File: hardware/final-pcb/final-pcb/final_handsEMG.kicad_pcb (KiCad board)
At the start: 2 copper layers, 109 parts, among them J1 Conn_02x13_Odd_Even, U1 ADS1299CPAG, U2 STM32L496ZGT6, U3 FT231XQ-R, U6 TPS60403DBVT, U8 TPS72325DBVT, U9 TPS73225DBVT

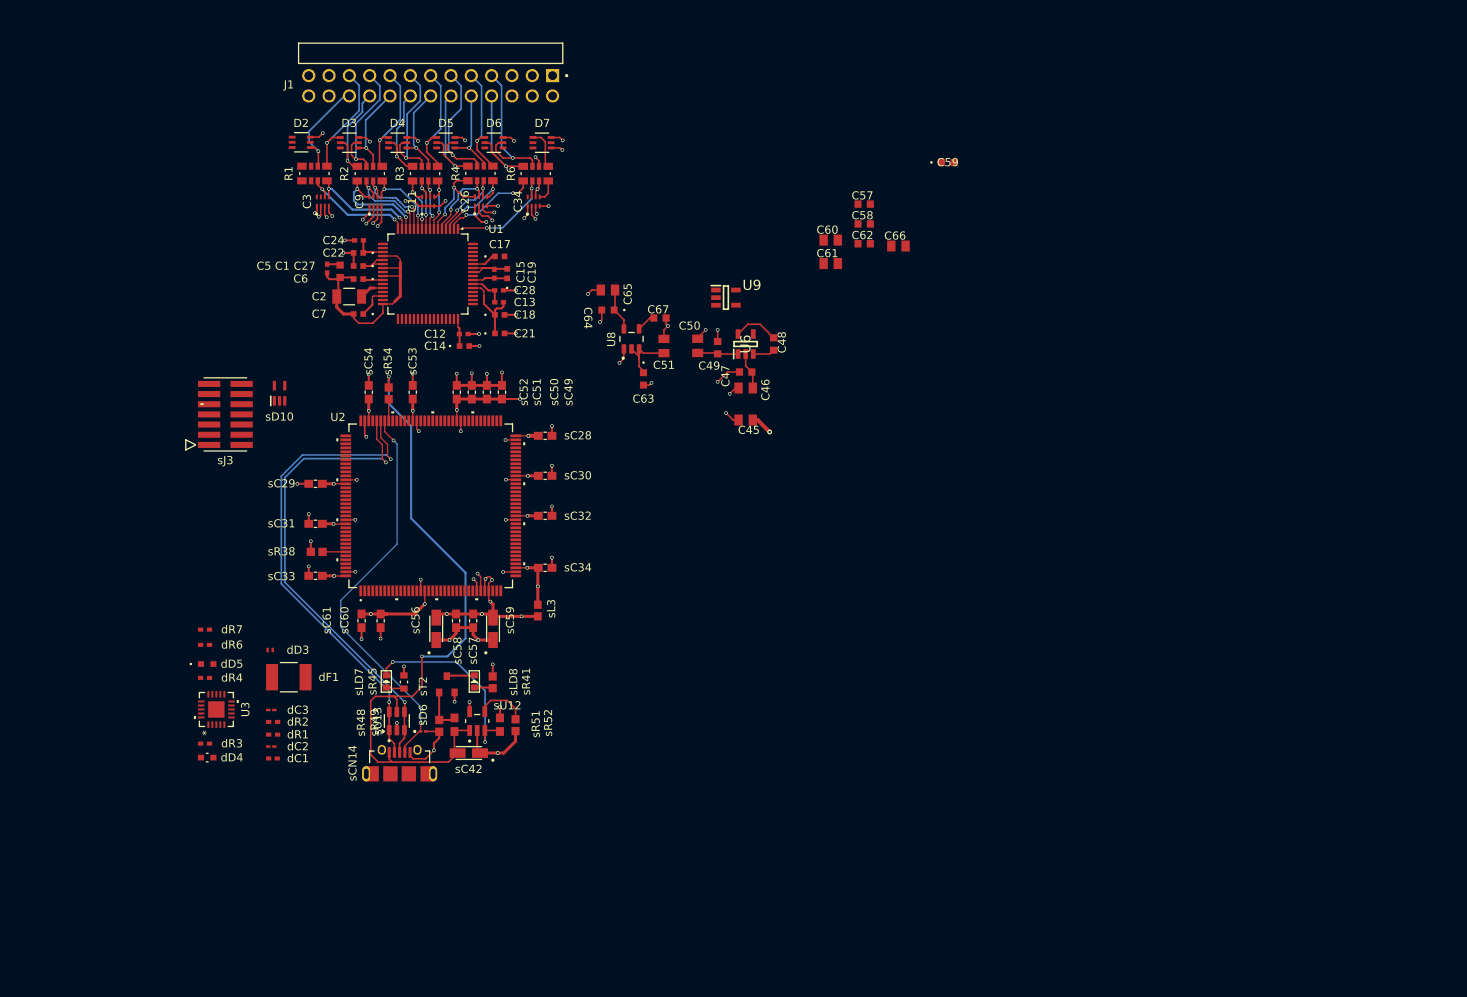
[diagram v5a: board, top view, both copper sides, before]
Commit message: 90% of components are placed (4.5.25)
NEED TESTPOINTS and configure the jumper parts for the PMIC without using jumpers
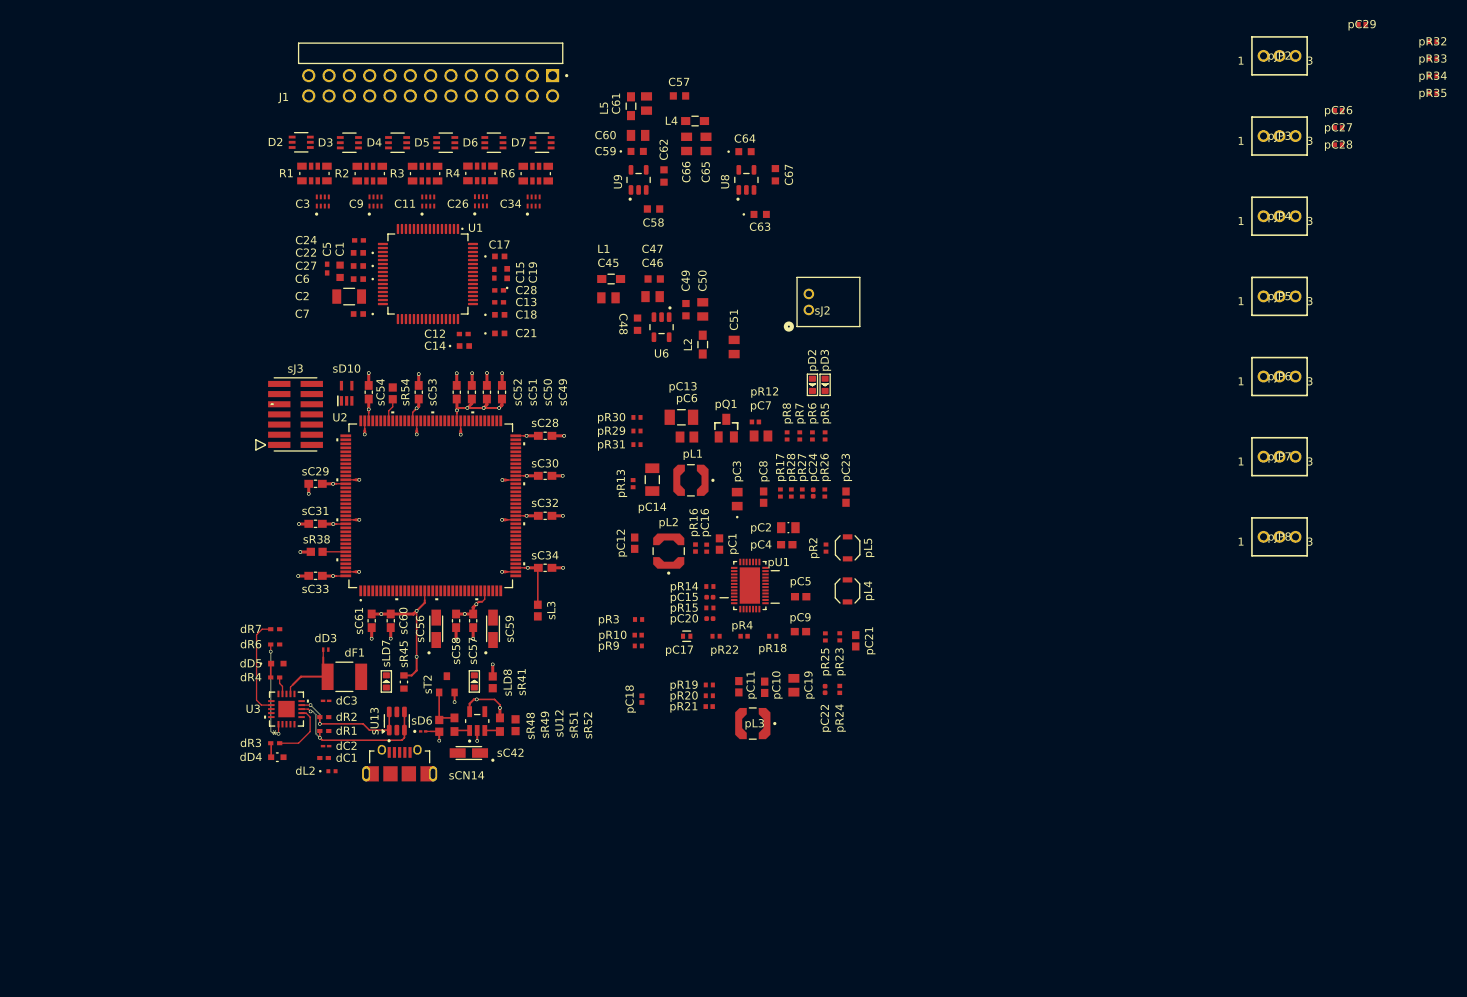
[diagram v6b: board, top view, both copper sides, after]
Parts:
- added L1: 3.3uH, MLZ2012A3R3W:INDC2012X87N, F.Cu at (128.4, 61.6)
- added L2: 3.3uH, MLZ2012A3R3W:INDC2012X87N, F.Cu at (139.8, 69.8)
- added L4: 3.3uH, MLZ2012A3R3W:INDC2012X87N, F.Cu at (138.9, 41.9)
- added L5: 3.3uH, MLZ2012A3R3W:INDC2012X87N, F.Cu at (130.9, 40.0)
- added dL2: L_Small, MPZ1005S300C:IND_1005_TDK, F.Cu at (93.5, 123.2)
- added pC1: 1uF, 03PowerFOOTPRINTS:C1005X5R0J105M, F.Cu at (141.9, 94.8)
- added pC10: 2.2uF, 03PowerFOOTPRINTS:C1608X5R0J225M, F.Cu at (147.6, 112.7)
- added pC11: 1uF, 03PowerFOOTPRINTS:C1005X5R0J105M, F.Cu at (144.4, 112.6)
- added pC12: 10uF, 03PowerFOOTPRINTS:C1608X5R0J106M, F.Cu at (131.3, 94.6)
- added pC13: 100uF, 03PowerFOOTPRINTS:GRM31CR60J107ME39L, F.Cu at (137.2, 78.9)
- added pC14: 47uF, 03PowerFOOTPRINTS:LMK316BJ476ML-T, F.Cu at (133.5, 86.7)
- added pC15: 10pF, 03PowerFOOTPRINTS:04025A100KAT, F.Cu at (140.7, 101.4)
- added pC16: 0.1uF, 03PowerFOOTPRINTS:C1005X5R1C104K, F.Cu at (140.3, 95.3)
- added pC17: 330pF, 03PowerFOOTPRINTS:04025A331KAT, F.Cu at (137.8, 106.3)
- added pC18: 33pF, 03PowerFOOTPRINTS:04025A330KAT, F.Cu at (132.2, 114.1)
- added pC19: 22uF, 03PowerFOOTPRINTS:JMK212BJ226MG-T, F.Cu at (151.2, 112.4)
- added pC2: 10uF, 03PowerFOOTPRINTS:GRM21BR61A106KE19, F.Cu at (150.6, 92.7)
- added pC20: 10pF, 03PowerFOOTPRINTS:04025A100KAT, F.Cu at (140.7, 104.1)
- added pC21: 10uF, 03PowerFOOTPRINTS:C1608X5R0J106M, F.Cu at (159.0, 106.8)
- added pC22: 10pF, 03PowerFOOTPRINTS:04025A100KAT, F.Cu at (155.1, 112.9)
- added pC23: 10uF, 03PowerFOOTPRINTS:C1608X5R0J106M, F.Cu at (157.8, 88.9)
- added pC24: 10pF, 03PowerFOOTPRINTS:04025A100KAT, F.Cu at (153.7, 88.4)
- added pC26: 0.1uF, 03PowerFOOTPRINTS:C1005X5R1C104K, F.Cu at (219.3, 40.5)
- added pC27: 0.1uF, 03PowerFOOTPRINTS:C1005X5R1C104K, F.Cu at (219.3, 42.7)
- added pC28: 0.1uF, 03PowerFOOTPRINTS:C1005X5R1C104K, F.Cu at (219.3, 44.8)
- added pC29: 0.1uF, 03PowerFOOTPRINTS:C1005X5R1C104K, F.Cu at (222.3, 29.8)
- added pC3: 10uF, 03PowerFOOTPRINTS:GRM21BR61A106KE19L, F.Cu at (144.2, 89.1)
- added pC4: 1uF, 03PowerFOOTPRINTS:C1005X5R0J105M, F.Cu at (150.4, 94.8)
- added pC5: 1uF, 03PowerFOOTPRINTS:C1005X5R0J105M, F.Cu at (152.1, 101.3)
- added pC6: 22uF, 03PowerFOOTPRINTS:JMK212BJ226MG-T, F.Cu at (137.9, 81.4)
- added pC7: 22uF, 03PowerFOOTPRINTS:JMK212BJ226MG-T, F.Cu at (147.1, 81.2)
- added pC8: 1uF, 03PowerFOOTPRINTS:C1005X5R0J105M, F.Cu at (147.5, 88.9)
- added pC9: 1uF, 03PowerFOOTPRINTS:C1005X5R0J105M, F.Cu at (152.1, 105.7)
- added pD2: GREEN (CHRG), SMD-LED-CLEAR-GREEN_0603_:LED-0603, F.Cu at (153.6, 74.8)
- added pD3: RED (FAULT), LED-SMD-RED-DIFFUSED_0603_:LED-0603, F.Cu at (155.1, 74.8)
- added pJP2: TMM-103-02-L-S, 03PowerFOOTPRINTS:SAMTEC-TMM-103-02-X-S, F.Cu at (212.0, 33.7)
- added pJP3: TMM-103-02-L-S, 03PowerFOOTPRINTS:SAMTEC-TMM-103-02-X-S, F.Cu at (212.0, 43.8)
- added pJP4: TMM-103-02-L-S, 03PowerFOOTPRINTS:SAMTEC-TMM-103-02-X-S, F.Cu at (212.0, 53.8)
- added pJP5: TMM-103-02-L-S, 03PowerFOOTPRINTS:SAMTEC-TMM-103-02-X-S, F.Cu at (212.0, 63.8)
- added pJP6: TMM-103-02-L-S, 03PowerFOOTPRINTS:SAMTEC-TMM-103-02-X-S, F.Cu at (212.0, 73.8)
- added pJP7: TMM-103-02-L-S, 03PowerFOOTPRINTS:SAMTEC-TMM-103-02-X-S, F.Cu at (212.0, 83.8)
- added pJP8: TMM-103-02-L-S, 03PowerFOOTPRINTS:SAMTEC-TMM-103-02-X-S, F.Cu at (212.0, 93.9)
- added pL1: 3.3uH, 03PowerFOOTPRINTS:LPS4018-332MLC, F.Cu at (138.4, 86.8)
- added pL2: 2.2uH, 03PowerFOOTPRINTS:LPS4018-222MLC, F.Cu at (135.6, 95.6)
- added pL3: 2.2uH, 03PowerFOOTPRINTS:LPS4018-222MLC, F.Cu at (146.1, 117.2)
- added pL4: 4.7uH, 03PowerFOOTPRINTS:IND_3010_TDK, F.Cu at (157.9, 100.6)
- added pL5: 4.7uH, 03PowerFOOTPRINTS:IND_3010_TDK, F.Cu at (158.0, 95.2)
- added pQ1: PMOS, 03PowerFOOTPRINTS:SI2333DS, F.Cu at (142.8, 80.3)
- added pR10: 0, 03PowerFOOTPRINTS:CRCW04020000Z0EDC, F.Cu at (131.8, 106.1)
- added pR12: 0, 03PowerFOOTPRINTS:CRCW04020000Z0EDC, F.Cu at (146.4, 79.5)
- added pR13: 20, 03PowerFOOTPRINTS:CRCW040220R0FKED, F.Cu at (131.1, 87.2)
- added pR14: 88.7k, 03PowerFOOTPRINTS:CRCW040288K7FKED, F.Cu at (140.7, 100.1)
- added pR15: 16.9K, 03PowerFOOTPRINTS:CRCW040216K9FKED, F.Cu at (140.7, 102.7)
- added pR16: 3.01K, 03PowerFOOTPRINTS:CRCW04023K01FKED, F.Cu at (138.9, 95.3)
- added pR17: 2K, 03PowerFOOTPRINTS:CRCW04022K00FKED, F.Cu at (149.6, 88.4)
- added pR18: 20, 03PowerFOOTPRINTS:CRCW040220R0FKED, F.Cu at (148.6, 106.3)
- added pR19: 15K, 03PowerFOOTPRINTS:CRCW040215K0FKED, F.Cu at (140.7, 112.4)
- added pR2: 1, 03PowerFOOTPRINTS:CRCW04021R00JNED, F.Cu at (155.3, 95.3)
- added pR20: 324K, 03PowerFOOTPRINTS:CRCW0402324KFKED, F.Cu at (140.7, 113.7)
- added pR21: 121K, 03PowerFOOTPRINTS:CRCW0402121KFKED, F.Cu at (140.7, 115.1)
- added pR22: 105K, 03PowerFOOTPRINTS:CRCW0402105KFKED, F.Cu at (141.5, 106.3)
- added pR23: 20, 03PowerFOOTPRINTS:CRCW040220R0FKED, F.Cu at (157.0, 106.4)
- added pR24: 806K, 03PowerFOOTPRINTS:CRCW0402806KFKED, F.Cu at (157.0, 112.9)
- added pR25: 649K, 03PowerFOOTPRINTS:CRCW0402649KFKED, F.Cu at (155.2, 106.4)
- added pR26: 20, 03PowerFOOTPRINTS:CRCW040220R0FKED, F.Cu at (155.1, 88.4)
- added pR27: 232K, 03PowerFOOTPRINTS:CRCW0402232KFKED, F.Cu at (152.3, 88.4)
- added pR28: 464K, 03PowerFOOTPRINTS:CRCW0402464KFKED, F.Cu at (150.9, 88.4)
- added pR29: 1, 03PowerFOOTPRINTS:CRCW04021R00JNED, F.Cu at (131.6, 80.6)
- added pR3: 100K, 03PowerFOOTPRINTS:CRCW0402100KFKED, F.Cu at (131.8, 104.2)
- added pR30: 1, 03PowerFOOTPRINTS:CRCW04021R00JNED, F.Cu at (131.6, 78.9)
- added pR31: 1, 03PowerFOOTPRINTS:CRCW04021R00JNED, F.Cu at (131.6, 82.3)
- added pR32: 1K, 03PowerFOOTPRINTS:CRCW04021K00JNED, F.Cu at (231.1, 31.9)
- added pR33: 1K, 03PowerFOOTPRINTS:CRCW04021K00JNED, F.Cu at (231.1, 34.1)
- added pR34: 1K, 03PowerFOOTPRINTS:CRCW04021K00JNED, F.Cu at (231.1, 36.2)
- added pR35: 1K, 03PowerFOOTPRINTS:CRCW04021K00JNED, F.Cu at (231.1, 38.4)
- added pR4: 0, 03PowerFOOTPRINTS:CRCW04020000Z0EDC, F.Cu at (145.0, 106.3)
- added pR5: 1K, 03PowerFOOTPRINTS:CRCW04021K00JNED, F.Cu at (155.1, 81.2)
- added pR6: 2.2K, 03PowerFOOTPRINTS:CRCW04022K20FKED, F.Cu at (153.6, 81.2)
- added pR7: 1K, 03PowerFOOTPRINTS:CRCW04021K00JNED, F.Cu at (152.0, 81.2)
- added pR8: 2.2K, 03PowerFOOTPRINTS:CRCW04022K20FKED, F.Cu at (150.4, 81.2)
- added pR9: 100K, 03PowerFOOTPRINTS:CRCW0402100KFKED, F.Cu at (131.8, 107.5)
- added pU1: LTC3586EUFE-3-PBF, 03PowerFOOTPRINTS:LTC3586EUFE, F.Cu at (145.7, 99.9)
- added sJ2: S2B-PH-K-SLFSN, S2B-PH-K-S:CONN_S2B-PH-K-S_JST, F.Cu at (153.1, 65.5)
- U9: footprint TPS60403DBVT:SOT95P280X145-5N -> TPS73225DBVT:SOT95P280X145-5N
- moved C59 38.8 mm to (131.7, 45.7)
- moved C61 30.5 mm to (132.8, 39.7), turned to -90 degrees
- moved C66 29.4 mm to (137.8, 44.7), turned to -90 degrees
- moved C60 27.4 mm to (131.8, 43.7)
- moved C57 26.8 mm to (136.9, 38.7)
- moved C62 26.4 mm to (135.0, 48.8), turned to -90 degrees
- moved C58 26.4 mm to (133.7, 52.9)
- moved C64 26.2 mm to (145.1, 45.7), turned to 0 degrees
- moved C63 25.2 mm to (147.0, 53.5), turned to 0 degrees
- moved U8 24.5 mm to (145.3, 49.2)
- moved C67 23.0 mm to (148.9, 48.6), turned to -90 degrees
- moved C45 23.0 mm to (128.1, 64.0), turned to 0 degrees
- moved C65 22.0 mm to (140.3, 44.7), turned to -90 degrees
- moved U9 18.3 mm to (131.8, 49.2), turned to 90 degrees
- moved C48 17.2 mm to (131.7, 67.3), turned to 90 degrees
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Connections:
- C45 pad 1: AVOUT4 -> 5VCC
- U2 pad 103: USB_DN -> PA11
- U2 pad 104: USB_DP -> PA12
- U2 pad 106: DVDD -> AVOUT3
- U2 pad 108: DVDD -> AVOUT3
- U2 pad 121: DVDD -> AVOUT3
- U2 pad 131: DVDD -> AVOUT3
- U2 pad 144: DVDD -> AVOUT3
- U2 pad 17: DVDD -> AVOUT3
- U2 pad 39: DVDD -> AVOUT3
- U2 pad 52: DVDD -> AVOUT3
- U2 pad 62: DVDD -> AVOUT3
- U2 pad 72: DVDD -> AVOUT3
- U2 pad 84: DVDD -> AVOUT3
- U2 pad 95: DVDD -> AVOUT3
- sC42 pad +: USB_VBUS -> (no net)
- sC42 pad -: GND -> (no net)
- sR54 pad 2: USB_VBUS -> AVBUS
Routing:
- net GNDA: track 94.1 -> 2.88 mm, vias 48 -> 2
- net USB_VBUS: track 82.7 -> 0.00 mm, vias 2 -> 0
- net AVOUT3: track 8.67 -> 69.0 mm, vias 4 -> 19
- net DVDD: track 51.9 -> 0.00 mm, vias 14 -> 0
- net PA10: track 50.1 -> 0.00 mm, vias 2 -> 0
- net AVSS: track 46.1 -> 0.00 mm
- net USB_DN: track 60.7 -> 16.1 mm
- net USB_DP: track 60.3 -> 20.1 mm
- net AVDD: track 37.0 -> 5.91 mm, vias 6 -> 2
- net Net-(sLD7-K): track 24.8 -> 1.95 mm, vias 2 -> 0
- net GND: track 62.7 -> 42.9 mm, vias 31 -> 28
- net 8N: track 18.9 -> 0.00 mm, vias 1 -> 0
- net 6N: track 17.9 -> 0.00 mm, vias 1 -> 0
- net 4N: track 17.3 -> 0.00 mm, vias 1 -> 0
- net 2N: track 17.2 -> 0.00 mm, vias 1 -> 0
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
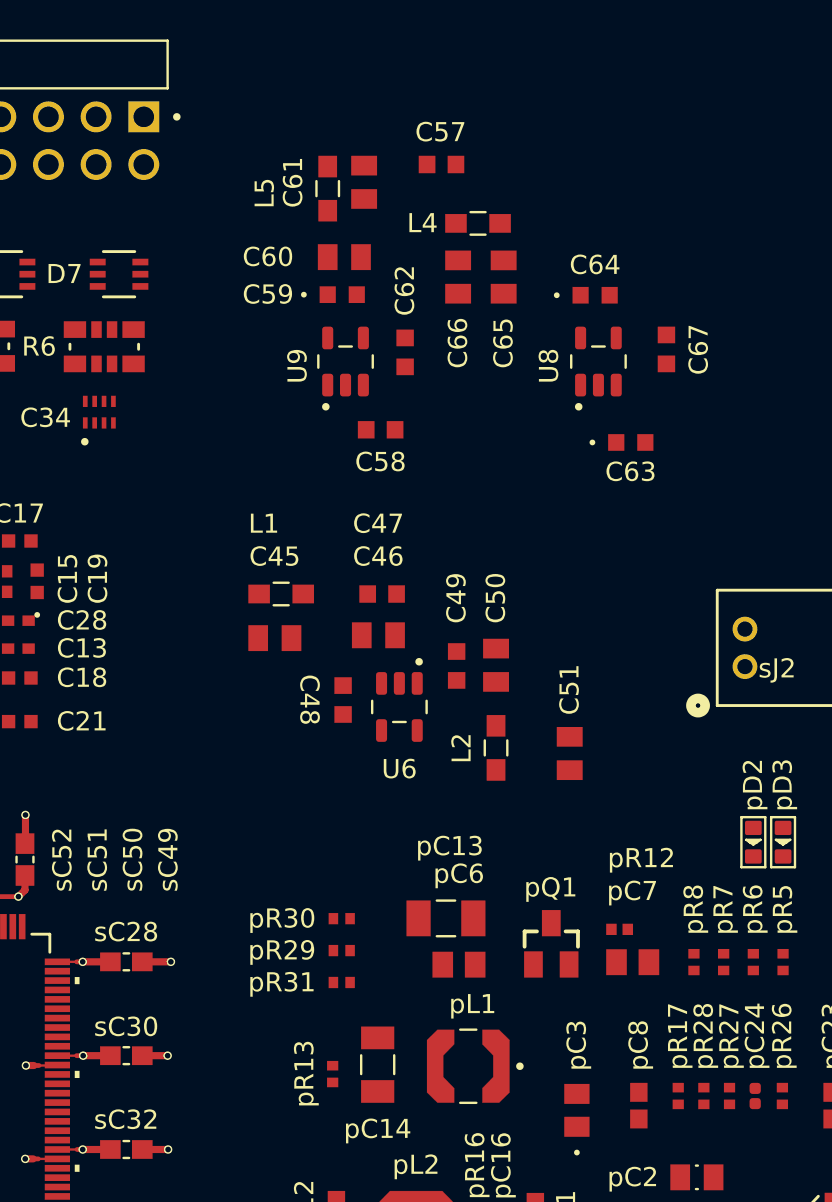
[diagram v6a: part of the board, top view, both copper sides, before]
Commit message: Changed flow of ADS power to easily flow from the Power portion
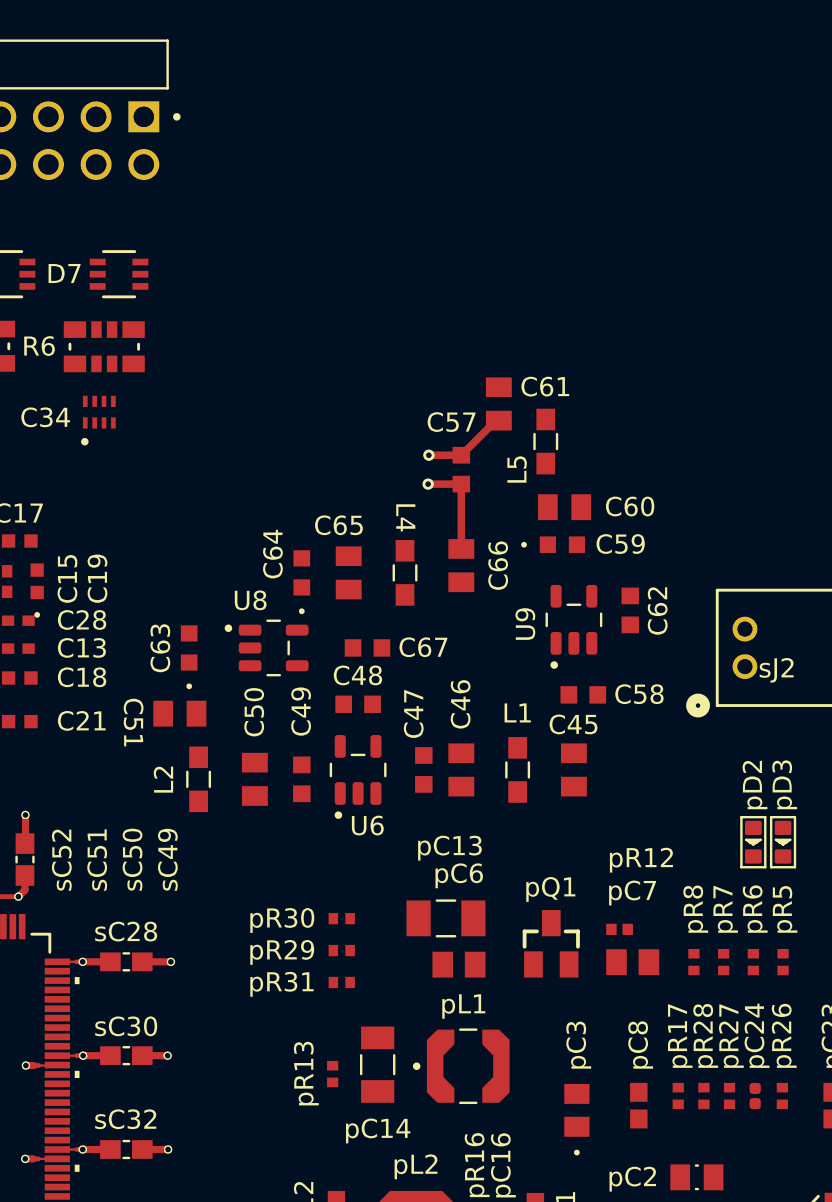
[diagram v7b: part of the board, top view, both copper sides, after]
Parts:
- moved C63 26.0 mm to (123.5, 64.5), turned to 90 degrees
- moved U8 23.1 mm to (128.0, 64.5), turned to 0 degrees
- moved C67 22.5 mm to (133.0, 64.5), turned to 0 degrees
- moved C64 21.5 mm to (129.5, 60.5), turned to 90 degrees
- moved C51 20.9 mm to (123.0, 68.0), turned to 180 degrees
- moved L4 19.0 mm to (135.0, 60.5), turned to 90 degrees
- moved U9 18.4 mm to (144.0, 63.0)
- moved C62 18.2 mm to (147.0, 62.5)
- moved C65 17.8 mm to (132.0, 60.5), turned to 90 degrees
- moved L5 17.8 mm to (142.5, 53.5)
- moved C58 17.8 mm to (144.5, 67.0)
- moved C59 17.8 mm to (143.4, 59.0)
- moved C60 17.8 mm to (143.5, 57.0)
- moved C45 17.4 mm to (144.0, 71.0), turned to -90 degrees
- moved C57 16.3 mm to (138.0, 55.0), turned to -90 degrees
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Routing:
- net AVSS: track 0.00 -> 5.22 mm, vias 0 -> 1
- net AVDD: track 5.91 -> 10.4 mm, vias 2 -> 3
